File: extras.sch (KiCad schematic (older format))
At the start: 16 parts, among them J41 μSD, J44 i2c, U42 24AA64-I_OT, U43 rtc_mc_rv_8263_c7

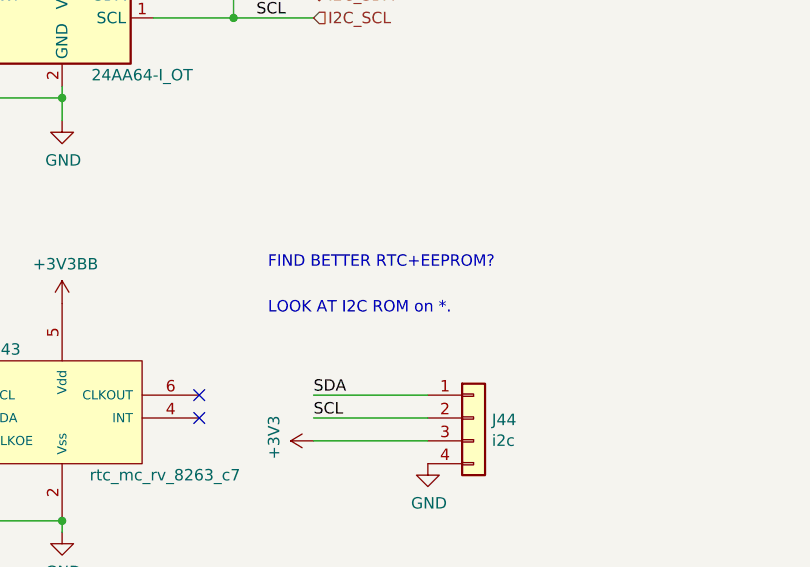
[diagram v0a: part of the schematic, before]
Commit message: Mk.3 fixes and new 68000 expansion board
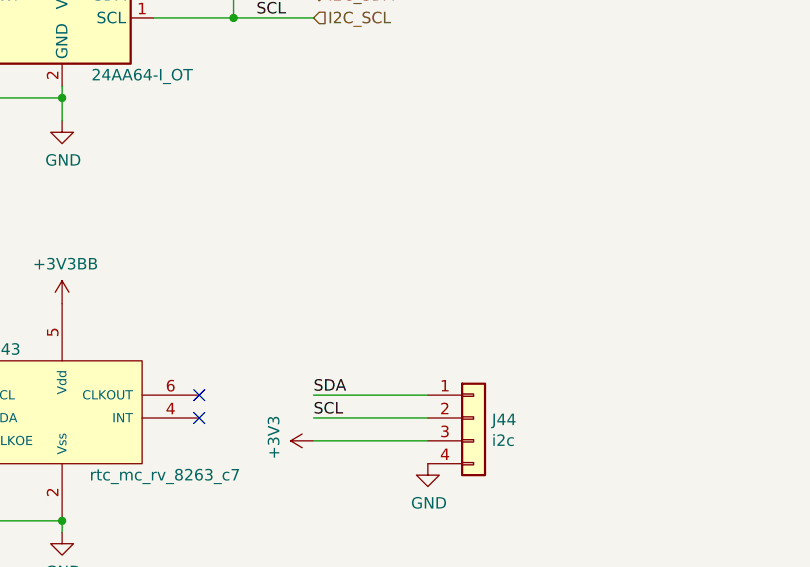
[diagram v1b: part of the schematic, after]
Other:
- note removed: "FIND BETTER RTC+EEPROM?\n"
- note removed: "LOOK AT I2C ROM on *."
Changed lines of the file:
@@
 Sheet 7 11
 Title "Mk.3 Blitter FPGA development board"
-Date "2021-05-08"
-Rev "3.00"
+Date "2021-08-14"
+Rev "3.03"
 Comp "Dossytronics"
-Comment1 ""
+Comment1 "fixed: clk/sysd0, jtag, u22 footprint"
 Comment2 ""
 Comment3 ""
@@
 Wire Wire Line
 	10550 3050 10550 2900
-Text Notes 3050 3350 0    50   ~ 0
-FIND BETTER RTC+EEPROM?\n
-Text Notes 3050 3550 0    50   ~ 0
-LOOK AT I2C ROM on *.
 Wire Wire Line
 	1050 4000 1550 4000
